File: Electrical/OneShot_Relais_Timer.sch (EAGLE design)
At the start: 26 parts, among them IC1 4511D, IC2 ATTINY204SOIC14, K1 Schrack RE030012, T1 BC847, X1 MKDSN1,5/2-5,08, X2 MKDSN1,5/2-5,08

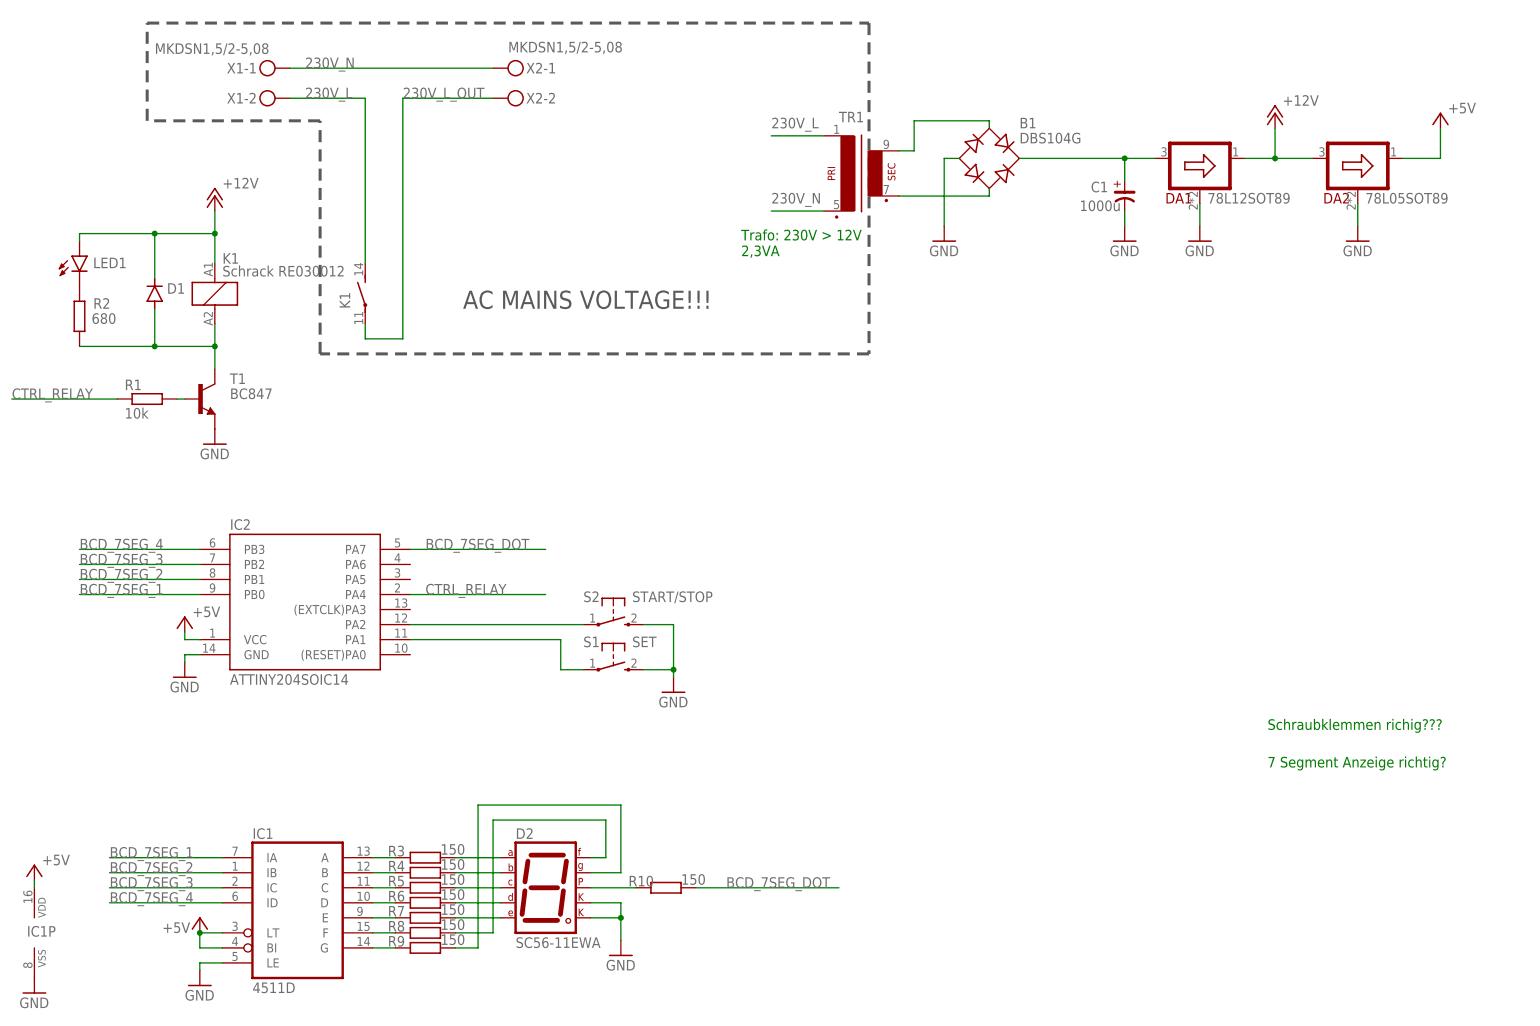
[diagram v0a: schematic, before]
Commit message: Replaced connectors for AC mains, replaced 12V regulator, added 3D models (trafo, relay, connector X1)
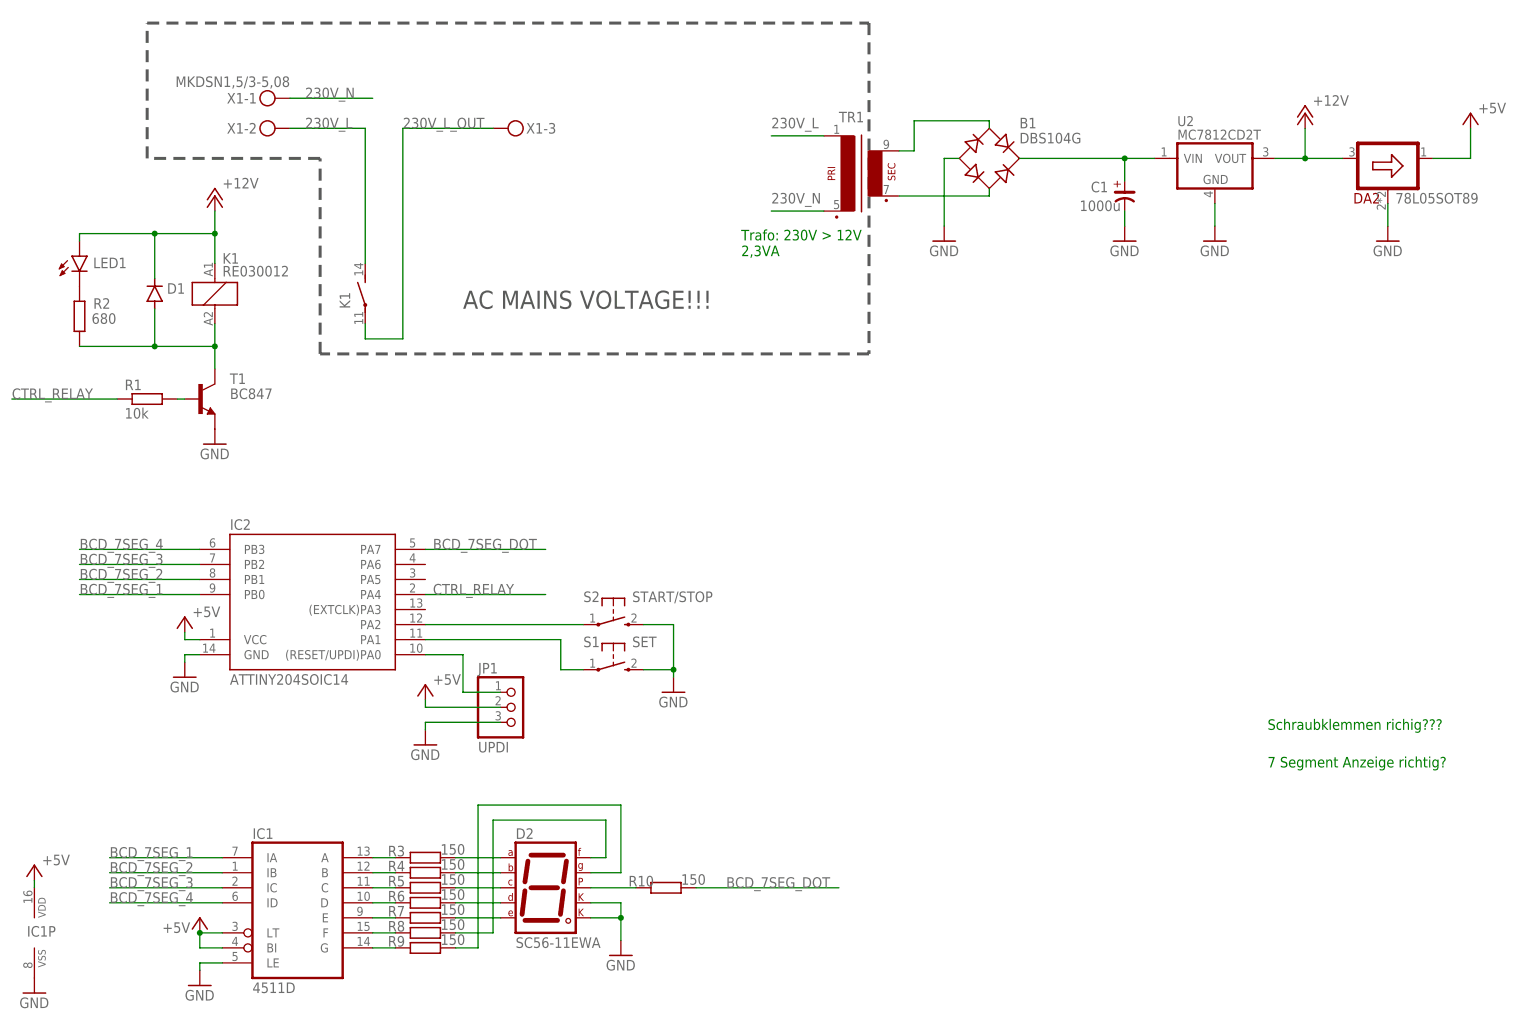
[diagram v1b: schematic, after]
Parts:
- removed DA1: 78L12SOT89, regulators-linear:78L12SOT89
- removed X2: MKDSN1,5/2-5,08, con-phoenix-508:MKDSN1,5/2-5,08
- added JP1: UPDI, pinhead:PINHD-1X3
- added U2: MC7812CD2T, _hhn_78xx_79xx_NCV78xx_d2pak_dpak:MC7812CD2T
- K1: value Schrack RE030012 -> RE030012; device relay:RE030012 -> OwnDevices:RE030012
- TR1: device trafo:EI30-1 -> OwnDevices:EI30-1
- X1: value MKDSN1,5/2-5,08 -> MKDSN1,5/3-5,08; device con-phoenix-508:MKDSN1,5/2-5,08 -> OwnDevices:MKDSN1,5/3-5,08
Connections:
- new net N$26: IC2.(RESET/UPDI)PA0, JP1.1
- net +12V: now also U2.VOUT; no longer DA1.OUT
- net +5V: now also JP1.2
- net 230V_L_OUT: now also X1-3.KL; no longer X2-2.KL
- net 230V_N: no longer X2-1.KL
- net GND: now also JP1.3, U2.GND; no longer DA1.GND
- net N$21: now also U2.VIN; no longer DA1.IN
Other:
- moved on the sheet: DA2, IC2, X1-1, X1-2

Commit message: Replaced 12V and 5V regulators, changed trafo type
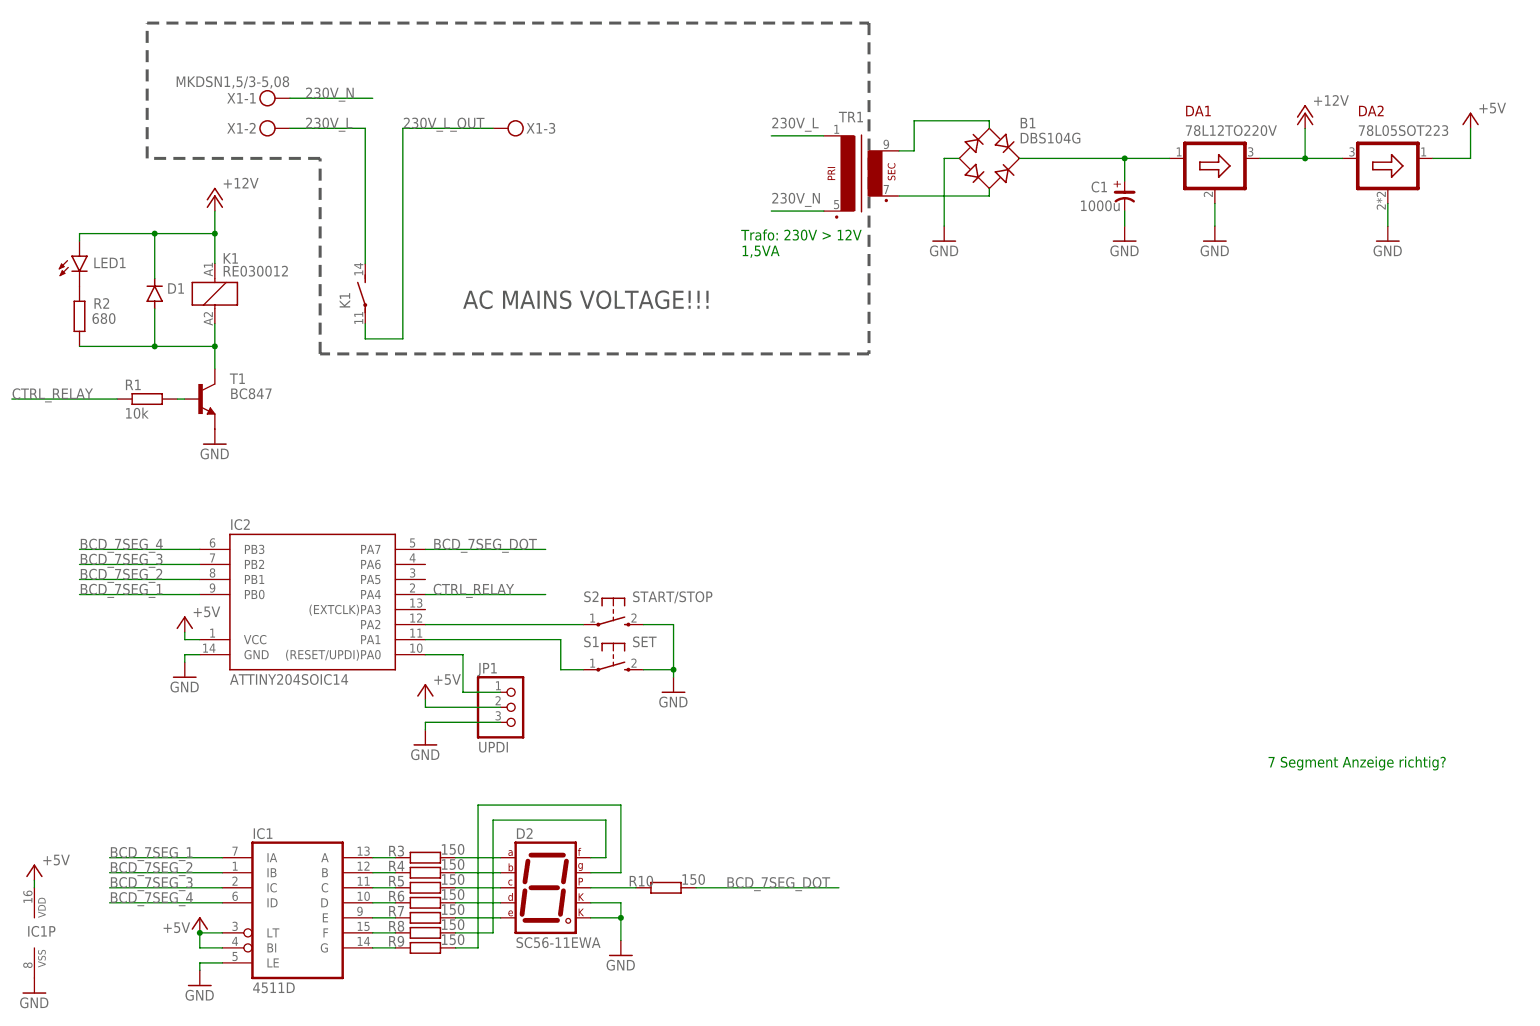
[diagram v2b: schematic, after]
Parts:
- removed U2: MC7812CD2T, _hhn_78xx_79xx_NCV78xx_d2pak_dpak:MC7812CD2T
- added DA1: 78L12TO220V, regulators-linear:78L12TO220V
- DA2: value 78L05SOT89 -> 78L05SOT223; device regulators-linear:78L05SOT89 -> regulators-linear:78L05SOT223
- TR1: device OwnDevices:EI30-1 -> OwnDevices:EI30-12.5
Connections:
- net +12V: now also DA1.OUT; no longer U2.VOUT
- net GND: now also DA1.GND; no longer U2.GND
- net N$21: now also DA1.IN; no longer U2.VIN
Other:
- note added: "Trafo: 230V > 12V 1,5VA"
- note removed: "Schraubklemmen richig???"
- note removed: "Trafo: 230V > 12V 2,3VA"
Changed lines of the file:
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@@
 <setting verticaltext="up"/>
 </settings>
-<grid distance="50" unitdist="mil" unit="mil" style="lines" multiple="1" display="no" altdistance="0.01" altunitdist="inch" altunit="inch"/>
+<grid distance="0.1" unitdist="inch" unit="inch" style="lines" multiple="1" display="no" altdistance="0.01" altunitdist="inch" altunit="inch"/>
 <layers>
 <layer number="1" name="Top" color="4" fill="1" visible="no" active="no"/>
@@
 <part name="GND6" library="supply1" library_urn="urn:adsk.eagle:library:371" deviceset="GND" device=""/>
 <part name="P+3" library="supply1" library_urn="urn:adsk.eagle:library:371" deviceset="+5V" device=""/>
-<part name="DA2" library="regulators-linear" deviceset="78L05" device="SOT89" value="78L05SOT89"/>
 <part name="P+5" library="supply1" library_urn="urn:adsk.eagle:library:371" deviceset="+12V" device=""/>
 <part name="P+6" library="supply1" library_urn="urn:adsk.eagle:library:371" deviceset="+5V" device=""/>
@@
 <part name="P+7" library="supply1" library_urn="urn:adsk.eagle:library:371" deviceset="+5V" device=""/>
 <part name="GND11" library="supply1" library_urn="urn:adsk.eagle:library:371" deviceset="GND" device=""/>
-<part name="U2" library="_hhn_78xx_79xx_NCV78xx_d2pak_dpak" deviceset="MC78*" device="D2T" technology="12C"/>
 <part name="K1" library="OwnDevices" library_urn="urn:adsk.eagle:library:19498084" deviceset="RE03*" device="" package3d_urn="urn:adsk.eagle:package:37656485/2" technology="0012"/>
 <part name="X1" library="OwnDevices" library_urn="urn:adsk.eagle:library:19498084" deviceset="MKDSN1,5/3-5,08" device="" package3d_urn="urn:adsk.eagle:package:37656663/2"/>
-<part name="TR1" library="OwnDevices" library_urn="urn:adsk.eagle:library:19498084" deviceset="EI30-1" device="" package3d_urn="urn:adsk.eagle:package:37656560/2"/>
+<part name="DA1" library="regulators-linear" deviceset="78L12" device="TO220V"/>
+<part name="DA2" library="regulators-linear" deviceset="78L05" device="SOT223"/>
+<part name="TR1" library="OwnDevices" library_urn="urn:adsk.eagle:library:19498084" deviceset="EI30-12.5" device="" package3d_urn="urn:adsk.eagle:package:37656560/4"/>
 </parts>
 <sheets>
 <sheet>
 <plain>
-<text x="217.17" y="52.07" size="1.778" layer="91">Schraubklemmen richig???</text>
 <text x="217.17" y="45.72" size="1.778" layer="91">7 Segment Anzeige richtig?</text>
 <text x="128.27" y="132.08" size="1.778" layer="91">Trafo: 230V &gt; 12V
-2,3VA</text>
+1,5VA</text>
 <wire x1="27.94" y1="171.45" x2="149.86" y2="171.45" width="0.508" layer="97" style="shortdash"/>
 <wire x1="149.86" y1="171.45" x2="149.86" y2="115.57" width="0.508" layer="97" style="shortdash"/>
@@
 <attribute name="VALUE" x="35.56" y="71.12" size="1.778" layer="96"/>
 </instance>
-<instance part="DA2" gate="G$1" x="237.49" y="148.59" smashed="yes">
-<attribute name="NAME" x="236.22" y="140.97" size="1.778" layer="94" rot="MR0"/>
-<attribute name="VALUE" x="238.76" y="140.97" size="1.778" layer="96"/>
-</instance>
 <instance part="P+5" gate="1" x="223.52" y="156.21" smashed="yes">
 <attribute name="VALUE" x="224.79" y="157.48" size="1.778" layer="96"/>
@@
 <attribute name="VALUE" x="72.39" y="46.99" size="1.778" layer="96"/>
 </instance>
-<instance part="U2" gate="G$1" x="208.28" y="148.59" smashed="yes">
-<attribute name="NAME" x="201.93" y="154.051" size="1.6764" layer="95"/>
-<attribute name="VALUE" x="201.93" y="151.765" size="1.6764" layer="96"/>
-</instance>
 <instance part="K1" gate="1" x="39.37" y="125.73" smashed="yes">
 <attribute name="VALUE" x="40.64" y="128.651" size="1.778" layer="96"/>
@@
 <instance part="X1" gate="-3" x="88.9" y="153.67" smashed="yes">
 <attribute name="NAME" x="91.948" y="152.781" size="1.778" layer="95"/>
+</instance>
+<instance part="DA1" gate="G$1" x="208.28" y="148.59" smashed="yes">
+<attribute name="NAME" x="203.2" y="157.48" size="1.778" layer="94" rot="MR180"/>
+<attribute name="VALUE" x="203.2" y="152.4" size="1.778" layer="96"/>
+</instance>
+<instance part="DA2" gate="G$1" x="237.49" y="148.59" smashed="yes">
+<attribute name="NAME" x="232.41" y="157.48" size="1.778" layer="94" rot="MR180"/>
+<attribute name="VALUE" x="232.41" y="152.4" size="1.778" layer="96"/>
 </instance>
 <instance part="TR1" gate="1" x="147.32" y="147.32" smashed="yes">
@@
 <pinref part="GND8" gate="1" pin="GND"/>
 <wire x1="208.28" y1="137.16" x2="208.28" y2="140.97" width="0.1524" layer="91"/>
-<pinref part="U2" gate="G$1" pin="GND"/>
+<pinref part="DA1" gate="G$1" pin="GND"/>
 </segment>
 <segment>
 <pinref part="GND7" gate="1" pin="GND"/>
+<wire x1="237.49" y1="137.16" x2="237.49" y2="140.97" width="0.1524" layer="91"/>
 <pinref part="DA2" gate="G$1" pin="GND"/>
-<wire x1="237.49" y1="137.16" x2="237.49" y2="140.97" width="0.1524" layer="91"/>
 </segment>
 <segment>
@@
 </segment>
 <segment>
-<pinref part="DA2" gate="G$1" pin="IN"/>
 <pinref part="P+5" gate="1" pin="+12V"/>
 <wire x1="223.52" y1="148.59" x2="229.87" y2="148.59" width="0.1524" layer="91"/>
 <wire x1="223.52" y1="153.67" x2="223.52" y2="148.59" width="0.1524" layer="91"/>
-<pinref part="U2" gate="G$1" pin="VOUT"/>
-<wire x1="218.44" y1="148.59" x2="223.52" y2="148.59" width="0.1524" layer="91"/>
 <junction x="223.52" y="148.59"/>
+<pinref part="DA1" gate="G$1" pin="OUT"/>
+<wire x1="215.9" y1="148.59" x2="223.52" y2="148.59" width="0.1524" layer="91"/>
+<pinref part="DA2" gate="G$1" pin="IN"/>
 </segment>
 </net>
@@
 <segment>
 <pinref part="P+6" gate="1" pin="+5V"/>
-<pinref part="DA2" gate="G$1" pin="OUT"/>
 <wire x1="251.46" y1="153.67" x2="251.46" y2="148.59" width="0.1524" layer="91"/>
 <wire x1="251.46" y1="148.59" x2="245.11" y2="148.59" width="0.1524" layer="91"/>
+<pinref part="DA2" gate="G$1" pin="OUT"/>
 </segment>
 <segment>
@@
 <segment>
 <pinref part="C1" gate="G$1" pin="+"/>
-<wire x1="198.12" y1="148.59" x2="193.04" y2="148.59" width="0.1524" layer="91"/>
+<wire x1="200.66" y1="148.59" x2="193.04" y2="148.59" width="0.1524" layer="91"/>
 <wire x1="193.04" y1="148.59" x2="193.04" y2="144.78" width="0.1524" layer="91"/>
 <pinref part="B1" gate="G$1" pin="+"/>
 <wire x1="175.26" y1="148.59" x2="193.04" y2="148.59" width="0.1524" layer="91"/>
 <junction x="193.04" y="148.59"/>
-<pinref part="U2" gate="G$1" pin="VIN"/>
-</segment>
-</net>
+<pinref part="DA1" gate="G$1" pin="IN"/>
+</segment>
+</net>

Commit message: Moved UI components (7 segment, buttons) to separate PCB
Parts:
- removed D2: SC56-11EWA, special:7SEG-CK
- removed IC1: 4511D, 45xx:4511D
- removed R10, R3, R4, R5, R6, R7, R8, R9: 150, OwnDevices:R-EU_R0805
- removed S1: SET, OwnDevices:KURZHUBTASTER
- removed S2: START/STOP, OwnDevices:KURZHUBTASTER
- added JP2: (no value), pinhead:PINHD-1X10
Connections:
- removed net N$10: IC1A.G, R9.1
- removed net N$11: D2.A, R3.2
- removed net N$12: D2.B, R4.2
- removed net N$13: D2.C, R5.2
- removed net N$14: D2.D, R6.2
- removed net N$15: D2.E, R7.2
- removed net N$16: D2.F, R8.2
- removed net N$17: D2.G, R9.2
- removed net N$18: IC2.PA2, S2.P
- removed net N$19: D2.DP, R10.1
- removed net N$20: IC2.PA1, S1.P
- removed net N$4: IC1A.A, R3.1
- removed net N$5: IC1A.B, R4.1
- removed net N$6: IC1A.C, R5.1
- removed net N$7: IC1A.D, R6.1
- removed net N$8: IC1A.E, R7.1
- removed net N$9: IC1A.F, R8.1
- new net BTN_SET: IC2.PA1, JP2.8
- new net BTN_START_STOP: IC2.PA2, JP2.7
- net +5V: now also JP2.1; no longer IC1A.BI, IC1A.LT, IC1P.VDD
- net BCD_7SEG_1: now also JP2.2; no longer IC1A.IA
- net BCD_7SEG_2: now also JP2.3; no longer IC1A.IB
- net BCD_7SEG_3: now also JP2.4; no longer IC1A.IC
- net BCD_7SEG_4: now also JP2.5; no longer IC1A.ID
- net BCD_7SEG_DOT: now also JP2.6; no longer R10.2
- net GND: now also JP2.10, JP2.9; no longer D2.CK1, D2.CK2, IC1A.LE, IC1P.VSS, S1.S, S2.S
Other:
- note removed: "7 Segment Anzeige richtig?"
